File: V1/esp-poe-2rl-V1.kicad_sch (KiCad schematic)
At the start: 56 parts, among them J1 USB_C_Receptacle_USB2.0, J2 RJ45 JACK, J3 1x2P 5,08mm, J4 1x2P 5,08mm, K1 G5NB-1A-E-DC5, K2 G5NB-1A-E-DC5, Q1 UMH3N, Q2 WPM2015-3/TR, Q3 LMUN2211LT1G, Q4 MMBT2222A, Q5 MMBT2222A, SW1 RESET, U4 CH340C, U5 ESP32-WROOM-32UE-N16, U6 LAN8710A

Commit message: Tweaks to components
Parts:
- added D10, D9: 1N4148, Tales:D_SOD-123, symbol Diode:1N4148
- C10, C11, C13, C14, C16, C17, C18, C20, C21, C23, R14, R15, R16, R17, R18, R19, R20, R21, R22, R23, R24, R25, R26, R27, R28, R29, R30: Case 0402/1005 -> (none); Package (none) -> 0402/1005
- C12, C15, C19, C25: Case 0603/1608 -> (none); Package (none) -> 0603/1608
- C22, C24: Case 1206/3216 -> (none); Package (none) -> 1206/3216
- D6: Case SOT-23-5 -> (none); Package (none) -> SOT-23-5
- D7, D8: Case 0603 -> (none); Package (none) -> 0603
- F1: Case 1206 -> (none); Package (none) -> 1206
- L3: Case 0805/2012 -> (none); Package (none) -> 0805/2012
- Q1: Case SOT-363 -> (none); Package (none) -> SOT-363
- Q2, Q3, Q4, Q5: Case SOT-23-3 -> (none); Package (none) -> SOT-23-3
- RN1, RN2, RN3: Case 4x0402 -> (none); Package (none) -> 4x0402
- SW1: Case SPST -> (none); Package (none) -> SPST
- U4: Case SOIC-16 -> (none); Package (none) -> SOIC-16
- U5: Case ESP32-WROOM-U -> (none); Package (none) -> ESP32-WROOM-U
- U6: Case QFN-32 -> (none); Package (none) -> QFN-32
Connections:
- net +5V: now also D10.1 (K), D9.1 (K)
- net at D8.1 (K), K2.4, Q5.3 (C): now also D10.2 (A)
- net at D7.1 (K), K1.4, Q4.3 (C): now also D9.2 (A)
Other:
- moved on the sheet: J3, J4, K1, K2

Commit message: Update image
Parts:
- J3, J4: footprint Tales:TerminalBlock_Dibo_DB142R-2-5.08_1x02_P5.08mm_Horizontal -> Tales:TerminalBlock_Dibo_DB142R-5.08-2P_1x02_P5.08mm_Horizontal
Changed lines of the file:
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@@
       (effects (font (size 1.27 1.27)) (justify left))
     )
-    (property "Footprint" "Tales:TerminalBlock_Dibo_DB142R-2-5.08_1x02_P5.08mm_Horizontal" (at 215.9 232.41 0)
+    (property "Footprint" "Tales:TerminalBlock_Dibo_DB142R-5.08-2P_1x02_P5.08mm_Horizontal" (at 215.9 232.41 0)
       (effects (font (size 1.27 1.27)) hide)
     )
@@
       (effects (font (size 1.27 1.27)) (justify left))
     )
-    (property "Footprint" "Tales:TerminalBlock_Dibo_DB142R-2-5.08_1x02_P5.08mm_Horizontal" (at 215.9 184.15 0)
-      (effects (font (size 1.27 1.27)) hide)
-    )
+    (property "Footprint" "Tales:TerminalBlock_Dibo_DB142R-5.08-2P_1x02_P5.08mm_Horizontal" (at 215.9 184.15 0)
+      (effects (font (size 1.27 1.27)) hide)
+    )

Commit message: Added temperature sensor
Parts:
- removed K1, K2: G5NB-1A-E-DC5, Tales:Relay_SPST_Omron_G5NB-1A, symbol Tales:G5NZ-1A
- added C26: 100nF/50V, Tales:C_0402_1005Metric, symbol Device:C_Small
- added K1, K2: G5NB-1A-E-DC5, Tales:Relay_SPST_Omron_G5NB-1A, symbol Tales:G5NB-1A
- added R31, R32: 2k2/62,5mW, Tales:R_0402_1005Metric, symbol Device:R_US
- added U7: AHT20, Tales:DFN-6-3x3mm_P1mm, symbol Tales:AHT20
- D10, D9: footprint Tales:D_SOD-123 -> Diode_THT:D_DO-35_SOD27_P7.62mm_Horizontal
- Q1: footprint Tales:SOT-363_SC-70-6 -> Package_TO_SOT_SMD:SOT-363_SC-70-6
- U4: footprint Tales:SOIC-16_3.9x9.9mm_P1.27mm -> Package_SO:SOIC-16_3.9x9.9mm_P1.27mm; symbol Interface_USB:CH340C -> Tales:CH340C
- U5: footprint Tales:ESP32-WROOM-32U -> RF_Module:ESP32-WROOM-32U
- U6: footprint Tales:QFN-32-1EP_5x5mm_P0.5mm_EP3.3x3.3mm_ThermalVias -> Package_DFN_QFN:QFN-32-1EP_5x5mm_P0.5mm_EP3.3x3.3mm_ThermalVias
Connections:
- net +3.3V: now also C26.1, R31.1, R32.1, U7.2 (VDD)
- net +5V: now also K1.1, K2.1
- net GND: now also C26.2, U7.5 (GND)
- net OUT1: now also U5.16 (IO13); no longer U5.9 (IO33)
- net OUT2: now also U5.27 (IO16); no longer U5.8 (IO32)
- net at D10.2 (A), D8.1 (K), Q5.3 (C): now also K2.4
- net at D7.1 (K), D9.2 (A), Q4.3 (C): now also K1.4
- net at J3.1 (Pin_1): now also K1.2
- net at J3.2 (Pin_2): now also K1.3
- net at J4.1 (Pin_1): now also K2.2
- net at J4.2 (Pin_2): now also K2.3
- new net I2C_SCL: R31.2, U5.8 (IO32), U7.3 (SCL)
- new net I2C_SDA: R32.2, U5.9 (IO33), U7.4 (SDA)
- no-connect marks 29 -> 27
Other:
- note added: "TEMP/HUMID ADDRESS 0x38"
- moved on the sheet: D10, D7, D8, D9, J3, J4, Q4, Q5, R25, R26, R27, R28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

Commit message: Added temperature sensor.
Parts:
- D10, D9: footprint Diode_THT:D_DO-35_SOD27_P7.62mm_Horizontal -> Tales:D_SOD-123
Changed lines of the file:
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@@
 			)
 		)
-		(property "Footprint" "Diode_THT:D_DO-35_SOD27_P7.62mm_Horizontal"
+		(property "Footprint" "Tales:D_SOD-123"
 			(at 142.24 248.92 0)
 			(effects
@@
 			)
 		)
-		(property "Footprint" "Diode_THT:D_DO-35_SOD27_P7.62mm_Horizontal"
+		(property "Footprint" "Tales:D_SOD-123"
 			(at 142.24 200.66 0)
 			(effects

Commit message: Reviewing board for fabrication
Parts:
- U5: footprint RF_Module:ESP32-WROOM-32U -> Tales:ESP32-WROOM-32U
- U6: footprint Package_DFN_QFN:QFN-32-1EP_5x5mm_P0.5mm_EP3.3x3.3mm_ThermalVias -> Tales:QFN-32-1EP_5x5mm_P0.5mm_EP3.3x3.3mm_ThermalVias
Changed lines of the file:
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@@
 			)
 		)
-		(property "Footprint" "RF_Module:ESP32-WROOM-32U"
+		(property "Footprint" "Tales:ESP32-WROOM-32U"
 			(at 181.61 133.35 0)
 			(effects
@@
 			)
 		)
-		(property "Footprint" "Package_DFN_QFN:QFN-32-1EP_5x5mm_P0.5mm_EP3.3x3.3mm_ThermalVias"
+		(property "Footprint" "Tales:QFN-32-1EP_5x5mm_P0.5mm_EP3.3x3.3mm_ThermalVias"
 			(at 312.42 129.54 0)
 			(effects

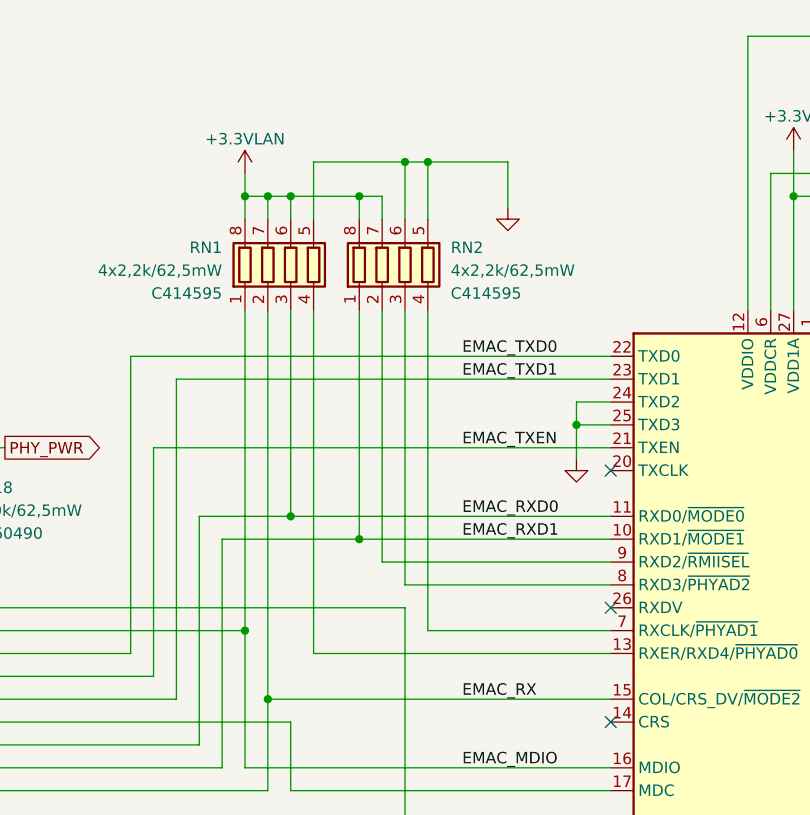
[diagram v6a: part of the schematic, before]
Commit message: Update esp-poe-2rl-V1.kicad_sch
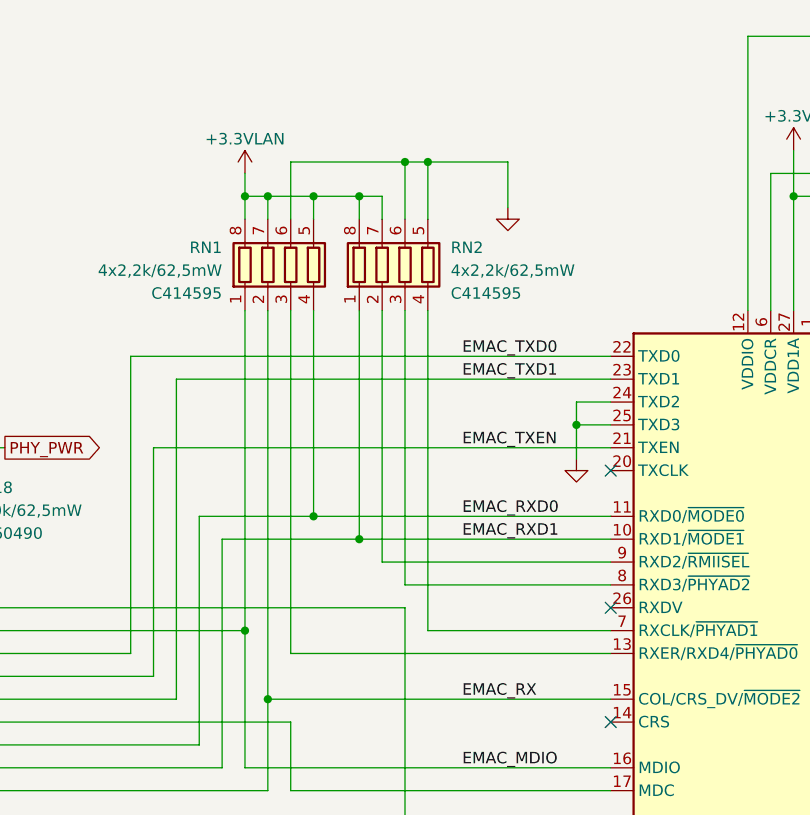
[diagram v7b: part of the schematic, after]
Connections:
- net +3.3VLAN: now also RN1.5 (R4.2); no longer RN1.6 (R3.2)
- net EMAC_RXD0: now also RN1.4 (R4.1); no longer RN1.3 (R3.1)
- net GND: now also RN1.6 (R3.2); no longer RN1.5 (R4.2)
- net at U6.13 (RXER/RXD4/~{PHYAD0}): now also RN1.3 (R3.1); no longer RN1.4 (R4.1)
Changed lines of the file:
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@@
 	)
 	(junction
-		(at 142.24 190.5)
+		(at 255.27 46.99)
 		(diameter 0)
 		(color 0 0 0 0)
 	)
 	(junction
-		(at 173.99 162.56)
+		(at 142.24 190.5)
 		(diameter 0)
 		(color 0 0 0 0)
 	)
 	(junction
-		(at 267.97 43.18)
+		(at 173.99 162.56)
 		(diameter 0)
 		(color 0 0 0 0)
 	)
 	(junction
-		(at 359.41 85.09)
+		(at 267.97 43.18)
 		(diameter 0)
 		(color 0 0 0 0)
 	)
 	(junction
-		(at 252.73 46.99)
+		(at 359.41 85.09)
 		(diameter 0)
 		(color 0 0 0 0)
@@
 	)
 	(junction
-		(at 252.73 82.55)
-		(diameter 0)
-		(color 0 0 0 0)
-	)
-	(junction
 		(at 245.11 132.08)
 		(diameter 0)
@@
 	)
 	(junction
+		(at 255.27 82.55)
+		(diameter 0)
+		(color 0 0 0 0)
+	)
+	(junction
 		(at 215.9 74.93)
 		(diameter 0)
@@
 	(wire
 		(pts
-			(xy 252.73 59.69) (xy 252.73 82.55)
+			(xy 255.27 59.69) (xy 255.27 82.55)
 		)
 		(stroke
@@
 	(wire
 		(pts
-			(xy 250.19 46.99) (xy 252.73 46.99)
+			(xy 250.19 46.99) (xy 255.27 46.99)
 		)
 		(stroke
@@
 	(wire
 		(pts
+			(xy 255.27 82.55) (xy 288.29 82.55)
+		)
+		(stroke
+			(width 0)
+			(type default)
+		)
+	)
+	(wire
+		(pts
 			(xy 68.58 58.42) (xy 68.58 81.28)
 		)
@@
 	(wire
 		(pts
+			(xy 255.27 46.99) (xy 255.27 49.53)
+		)
+		(stroke
+			(width 0)
+			(type default)
+		)
+	)
+	(wire
+		(pts
 			(xy 328.93 72.39) (xy 359.41 72.39)
 		)
@@
 	(wire
 		(pts
+			(xy 252.73 43.18) (xy 265.43 43.18)
+		)
+		(stroke
+			(width 0)
+			(type default)
+		)
+	)
+	(wire
+		(pts
 			(xy 57.15 68.58) (xy 59.69 68.58)
 		)
@@
 	(wire
 		(pts
-			(xy 142.24 259.08) (xy 158.75 259.08)
+			(xy 252.73 97.79) (xy 252.73 59.69)
 		)
 		(stroke
@@
 	(wire
 		(pts
-			(xy 240.03 67.31) (xy 288.29 67.31)
+			(xy 142.24 259.08) (xy 158.75 259.08)
 		)
 		(stroke
@@
 	(wire
 		(pts
-			(xy 106.68 40.64) (xy 99.06 40.64)
+			(xy 240.03 67.31) (xy 288.29 67.31)
 		)
 		(stroke
@@
 	(wire
 		(pts
-			(xy 252.73 82.55) (xy 288.29 82.55)
+			(xy 106.68 40.64) (xy 99.06 40.64)
 		)
 		(stroke
@@
 	(wire
 		(pts
-			(xy 255.27 43.18) (xy 265.43 43.18)
-		)
-		(stroke
-			(width 0)
-			(type default)
-		)
-	)
-	(wire
-		(pts
 			(xy 262.89 87.63) (xy 288.29 87.63)
 		)
@@
 	(wire
 		(pts
+			(xy 255.27 46.99) (xy 260.35 46.99)
+		)
+		(stroke
+			(width 0)
+			(type default)
+		)
+	)
+	(wire
+		(pts
 			(xy 147.32 85.09) (xy 147.32 88.9)
 		)
@@
 	(wire
 		(pts
-			(xy 255.27 59.69) (xy 255.27 97.79)
-		)
-		(stroke
-			(width 0)
-			(type default)
-		)
-	)
-	(wire
-		(pts
 			(xy 59.69 71.12) (xy 66.04 71.12)
 		)
@@
 	(wire
 		(pts
-			(xy 242.57 82.55) (xy 252.73 82.55)
+			(xy 242.57 82.55) (xy 255.27 82.55)
 		)
 		(stroke
@@
 	(wire
 		(pts
-			(xy 252.73 46.99) (xy 252.73 49.53)
-		)
-		(stroke
-			(width 0)
-			(type default)
-		)
-	)
-	(wire
-		(pts
 			(xy 245.11 110.49) (xy 245.11 85.09)
 		)
@@
 	(wire
 		(pts
-			(xy 252.73 46.99) (xy 260.35 46.99)
-		)
-		(stroke
-			(width 0)
-			(type default)
-		)
-	)
-	(wire
-		(pts
 			(xy 25.4 173.99) (xy 25.4 179.07)
 		)
@@
 	(wire
 		(pts
-			(xy 255.27 97.79) (xy 288.29 97.79)
-		)
-		(stroke
-			(width 0)
-			(type default)
-		)
-	)
-	(wire
-		(pts
 			(xy 204.47 52.07) (xy 204.47 54.61)
 		)
@@
 	(wire
 		(pts
-			(xy 255.27 43.18) (xy 255.27 49.53)
+			(xy 252.73 43.18) (xy 252.73 49.53)
 		)
 		(stroke
@@
 		)
 		(stroke
+			(width 0)
+			(type default)
+		)
+	)
+	(wire
+		(pts
+			(xy 252.73 97.79) (xy 288.29 97.79)
+		)
+		(stroke

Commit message: Preparations for fabrication
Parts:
- U7: JLCPCB BOM (none) -> 1; LCSC Part # (none) -> C2757850; Mfr (none) -> Aosong; Mfr PN (none) -> AHT20; Vendor (none) -> JLCPCB; Vendor PN (none) -> C2757850
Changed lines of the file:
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@@
+			)
+		)
+		(property "JLCPCB BOM" "1"
+			(at 195.58 162.56 0)
+			(effects
+				(font
+					(size 1.27 1.27)
+				)
+				(hide yes)
+			)
+		)
+		(property "LCSC Part #" "C2757850"
+			(at 195.58 162.56 0)
+			(effects
+				(font
+					(size 1.27 1.27)
+				)
+				(hide yes)
+			)
+		)
+		(property "Mfr" "Aosong"
+			(at 195.58 162.56 0)
+			(effects
+				(font
+					(size 1.27 1.27)
+				)
+				(hide yes)
+			)
+		)
+		(property "Mfr PN" "AHT20"
+			(at 195.58 162.56 0)
+			(effects
+				(font
+					(size 1.27 1.27)
+				)
+				(hide yes)
+			)
+		)
+		(property "Technology" "~"
+			(at 195.58 162.56 0)
+			(effects
+				(font
+					(size 1.27 1.27)
+				)
+				(hide yes)
+			)
+		)
+		(property "Vendor" "JLCPCB"
+			(at 195.58 162.56 0)
+			(effects
+				(font
+					(size 1.27 1.27)
+				)
+				(hide yes)
+			)
+		)
+		(property "Vendor PN" "C2757850"
+			(at 195.58 162.56 0)
+			(effects
+				(font
+					(size 1.27 1.27)
+				)
+				(hide yes)
 			)
 		)
